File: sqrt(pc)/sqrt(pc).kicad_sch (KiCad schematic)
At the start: 14 parts, among them U1 WEMOS_C3_mini

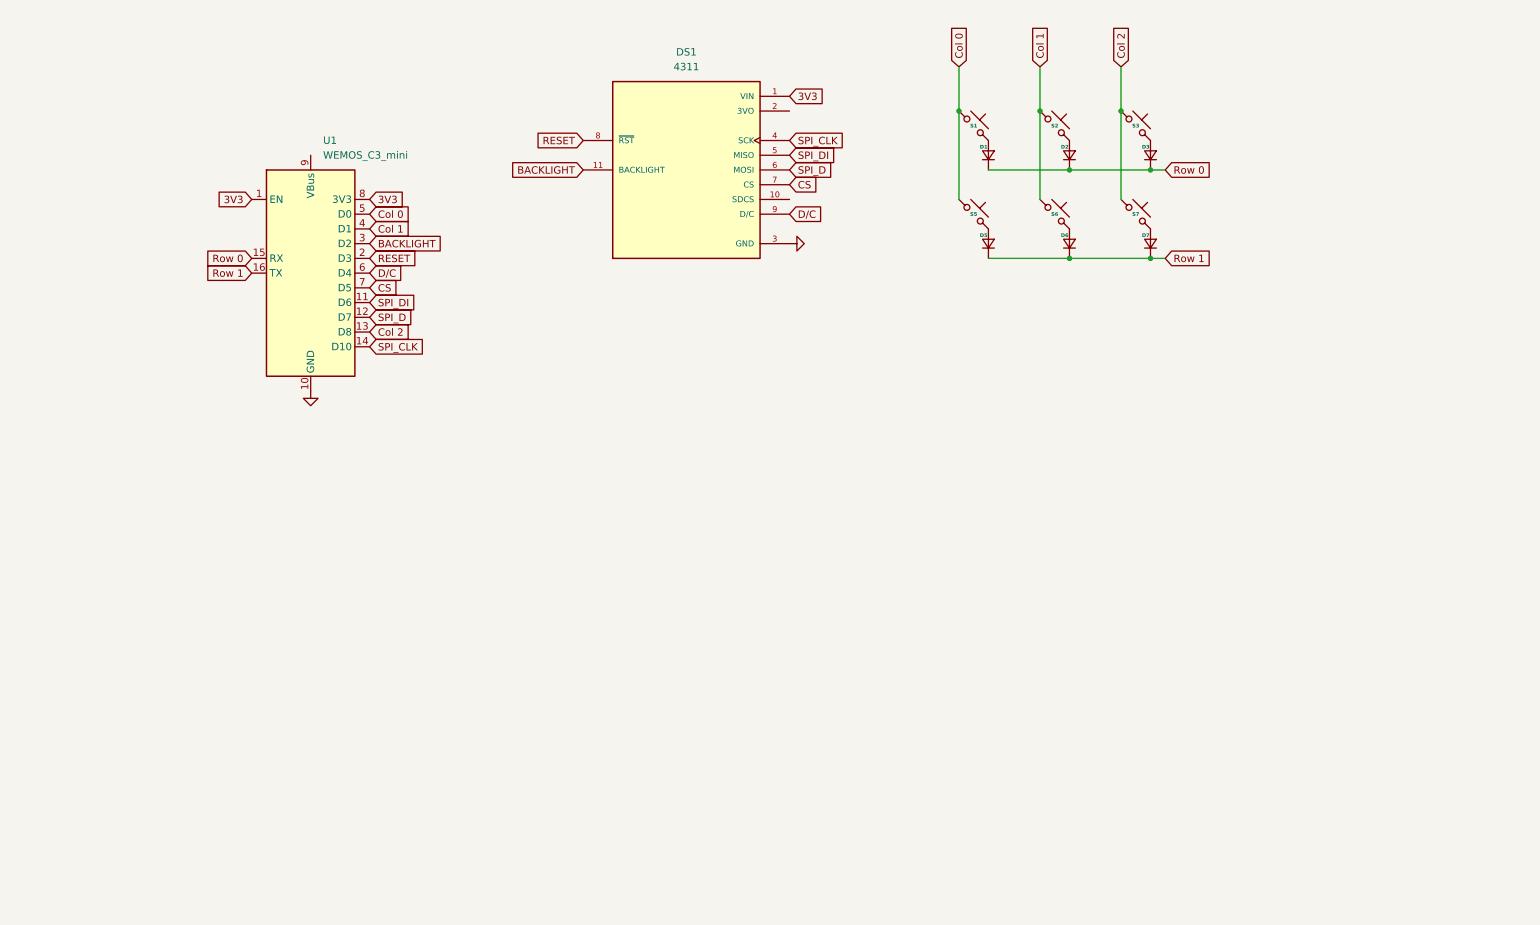
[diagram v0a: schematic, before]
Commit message: finished wiring PCB
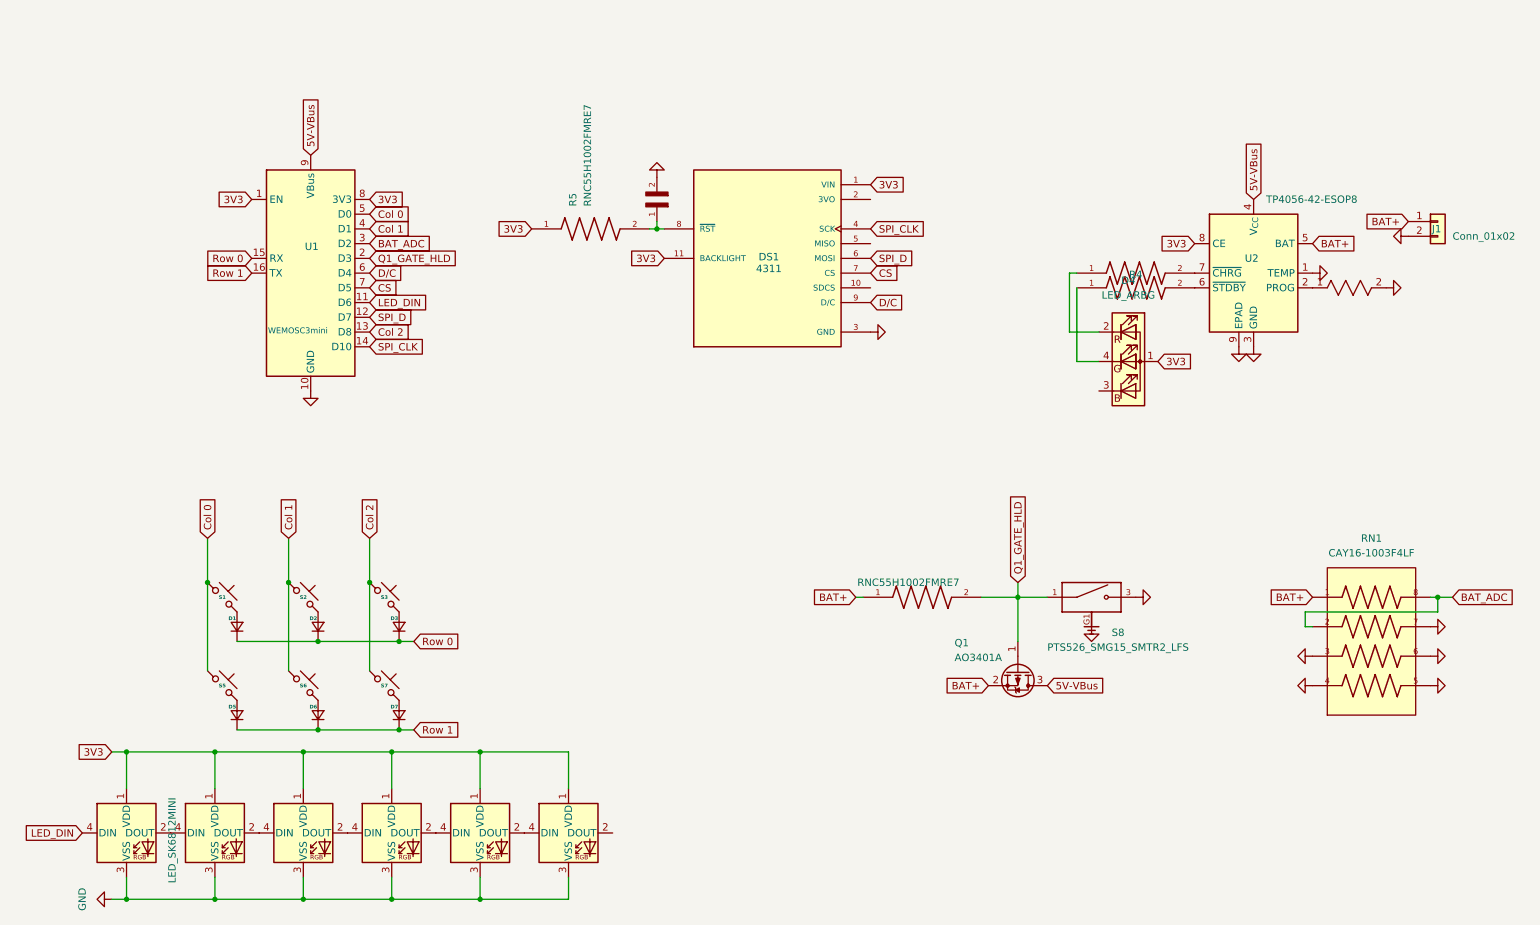
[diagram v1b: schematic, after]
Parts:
- added C46: 100nF, C315C104K5R5TA:CAPRR254W54L381T254H466B, symbol C315C104K5R5TA:C315C104K5R5TA
- added D10, D11, D12, D13, D14, D9: LED_SK6812MINI, ScottoKeebs_Components:LED_SK6812MINI, symbol ScottoKeebs:LED_SK6812MINI
- added D4: LED_ARBG, LED_SMD:LED_Kingbright_AAA3528ESGCT, symbol Device:LED_ARBG
- added J1: Conn_01x02, Connector_JST:JST_PH_B2B-PH-K_1x02_P2.00mm_Vertical, symbol Connector_Generic:Conn_01x02
- added Q1: AO3401A, Package_TO_SOT_SMD:SOT-23W_Handsoldering, symbol Transistor_FET:AO3401A
- added R2: FMP100JR-52-2K2, KiCADv6:FMP100JR_52_2K2, symbol FMP100JR_52_2K2:FMP100JR-52-2K2
- added R3, R4: MFR-25FBF52-1K, MFR-25FBF52-1K:RESAD1100W55L680D260, symbol MFR-25FBF52-1K:MFR-25FBF52-1K
- added R5, R6: RNC55H1002FMRE7, RNC55H1002FMRE7:RESAD1081W64L635D269, symbol RNC55H1002FMRE7:RNC55H1002FMRE7
- added RN1: CAY16-1003F4LF, CAY16-1003F4LF:RESCAF80P320X160X60-8N, symbol CAY16-1003F4LF:CAY16-1003F4LF
- added S8: PTS526_SMG15_SMTR2_LFS, PTS526_SMG15_SMTR2_LFS:SW_PTS526_SMG15_SMTR2_LFS, symbol PTS526_SMG15_SMTR2_LFS:PTS526_SMG15_SMTR2_LFS
- added U2: TP4056-42-ESOP8, Package_SO:SOIC-8-1EP_3.9x4.9mm_P1.27mm_EP2.41x3.3mm, symbol Battery_Management:TP4056-42-ESOP8
- U1: value WEMOS_C3_mini -> WEMOSC3mini
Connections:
- net 3V3: now also DS1.11 (BACKLIGHT), D10.1 (VDD), D11.1 (VDD), D12.1 (VDD), D13.1 (VDD), D14.1 (VDD), D4.1 (A), D9.1 (VDD), R5.1, U2.8 (CE)
- net GND: now also C46.2, D10.3 (VSS), D11.3 (VSS), D12.3 (VSS), D13.3 (VSS), D14.3 (VSS), D9.3 (VSS), J1.2 (Pin_2), R2.2, RN1.3, RN1.4, RN1.5, RN1.6, RN1.7, S8.3, S8.4, S8.G1, S8.G2, U2.1 (TEMP), U2.3 (GND), U2.9 (EPAD)
- net 5V-VBus: now reaches U1.9 (VBus)
- net 5V-VBus: now also Q1.3 (D), U2.4 (V_{CC})
- net BACKLIGHT renamed BAT_ADC
- net BAT_ADC: now also RN1.2, RN1.8; no longer DS1.11 (BACKLIGHT)
- net RESET: no longer names the net of DS1.8 (~{RST})
- net RESET: now also C46.1, R5.2; no longer U1.2 (D3)
- net SPI_DI: no longer names the net of DS1.5 (MISO)
- net SPI_DI: no longer U1.11 (D6)
- new net: D10.2 (DOUT), D9.4 (DIN)
- new net: D13.2 (DOUT), D14.4 (DIN)
- new net: D4.4 (GK), R3.1
- new net: R3.2, U2.6 (~{STDBY})
- new net: D4.2 (RK), R4.1
- new net: R2.1, U2.2 (PROG)
- new net: R4.2, U2.7 (~{CHRG})
- new net: D12.2 (DOUT), D13.4 (DIN)
- new net: D11.2 (DOUT), D12.4 (DIN)
- new net: D11.4 (DIN), D9.2 (DOUT)
- new net BAT+: J1.1 (Pin_1), Q1.2 (S), R6.1, RN1.1, U2.5 (BAT)
- new net LED_DIN: D10.4 (DIN), U1.11 (D6)
- new net Q1_GATE_HLD: Q1.1 (G), R6.2, S8.1, S8.2, U1.2 (D3)
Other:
- moved on the sheet: D1, D2, D3, D5, D6, D7, DS1, S1, S2, S3, S5, S6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

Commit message: BOM + a lot more I guess
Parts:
- J1: footprint Connector_JST:JST_PH_B2B-PH-K_1x02_P2.00mm_Vertical -> Connector_Molex:Molex_PicoBlade_53048-0210_1x02_P1.25mm_Horizontal
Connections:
- net LED_DIN: now also D9.4 (DIN); no longer D10.4 (DIN)
- net at D10.2 (DOUT): now also D11.4 (DIN); no longer D9.4 (DIN)
- net at D9.2 (DOUT): now also D10.4 (DIN); no longer D11.4 (DIN)
